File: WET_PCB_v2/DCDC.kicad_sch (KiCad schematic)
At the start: 8 parts, among them Q5 Q_NMOS_GDS, Q6 Q_NMOS_GDS

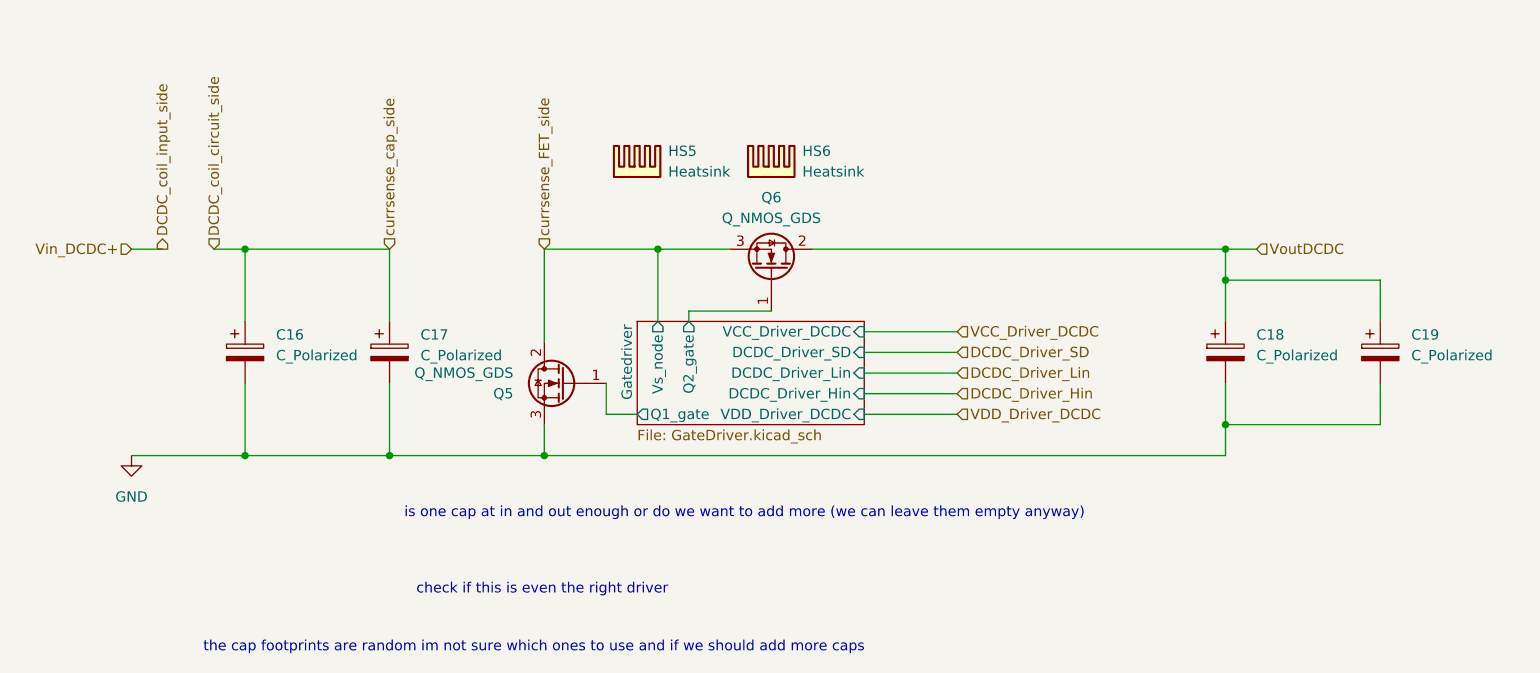
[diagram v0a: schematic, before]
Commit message: some caps were missing and wrong way around AAAAAAAAAAAAAAAAAAAAAAAAAAAAAAAAAAA
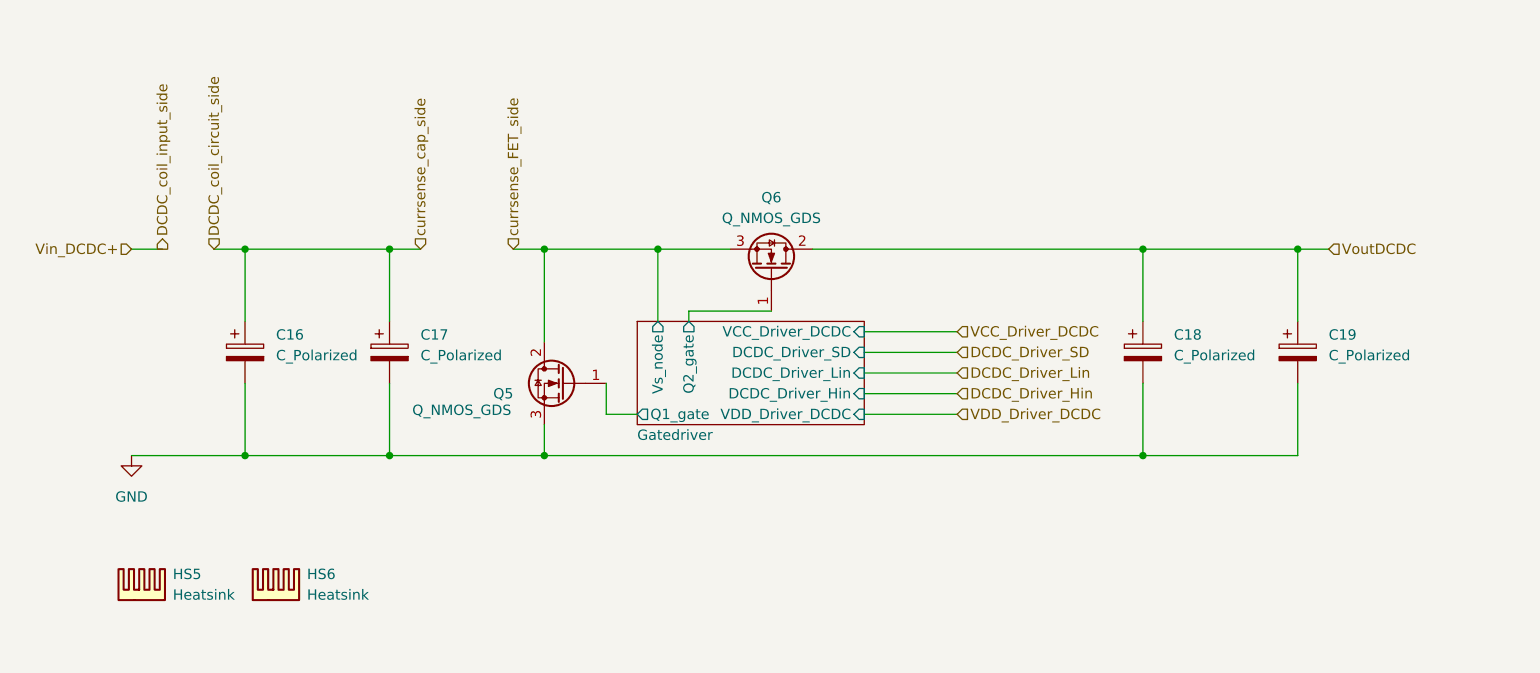
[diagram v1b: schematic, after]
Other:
- note removed: "check if this is even the right driver"
- note removed: "is one cap at in and out enough or do we want to add more (we can leave them empty anyway)"
- note removed: "the cap footprints are random im not sure which ones to use and if we should add more caps"
- moved on the sheet: C18, C19, HS5, HS6

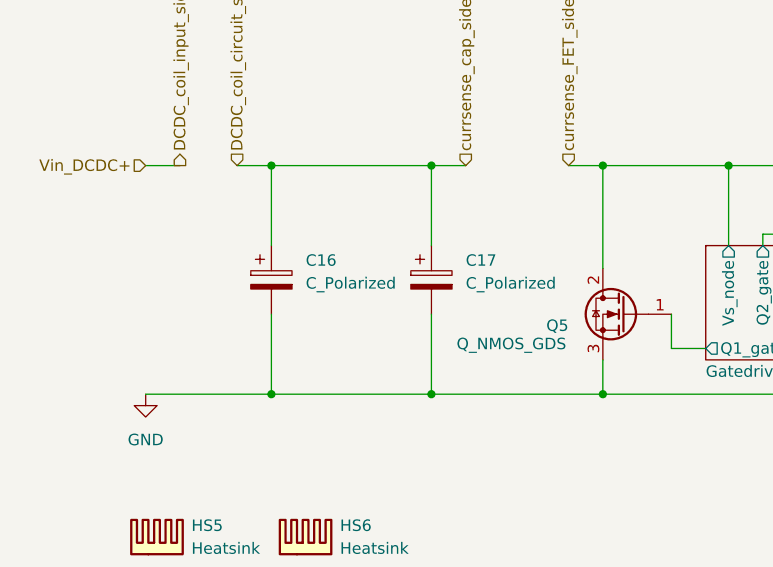
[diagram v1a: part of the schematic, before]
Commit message: added values and notes for assembly
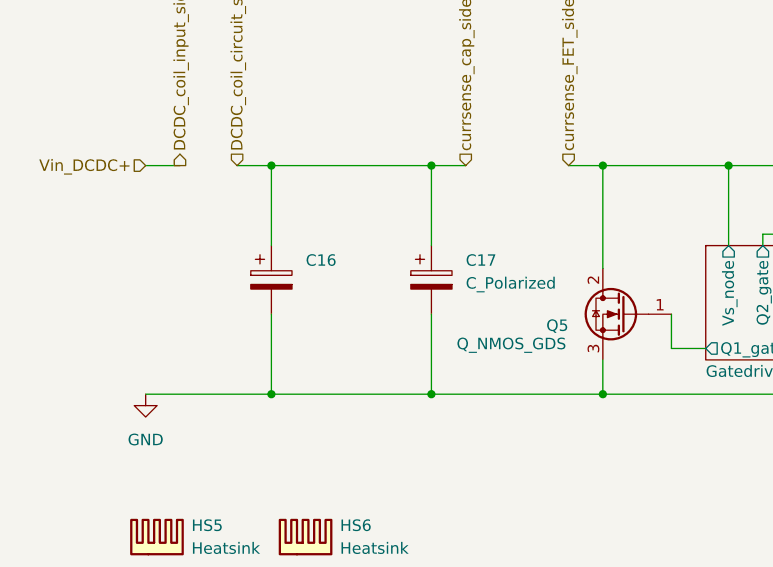
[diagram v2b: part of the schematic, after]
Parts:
- C16: value C_Polarized -> (none)
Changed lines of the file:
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@@
 			)
 		)
-		(property "Value" "C_Polarized"
+		(property "Value" ""
 			(at 58.42 56.2609 0)
 			(show_name no)
